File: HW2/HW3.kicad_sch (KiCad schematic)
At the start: 14 parts, among them SW1 SW_Push, SW2 SW_Push, U1 PIC32MX170F256B, U2 AP7381-33, U3 USB-UART

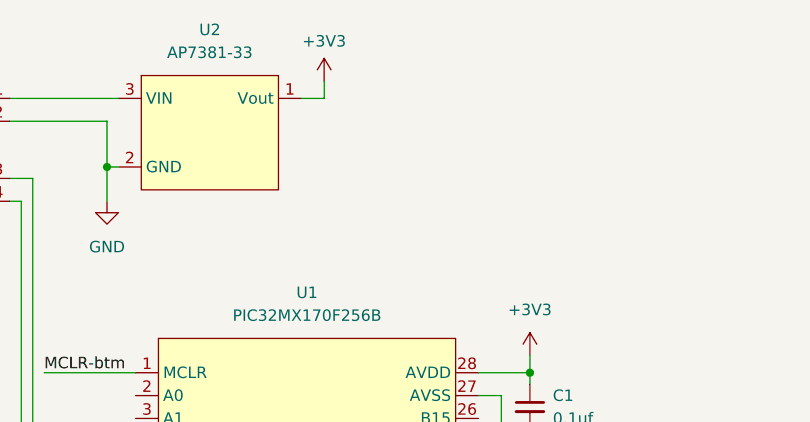
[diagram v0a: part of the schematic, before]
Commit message: HW4 question answered except for last one
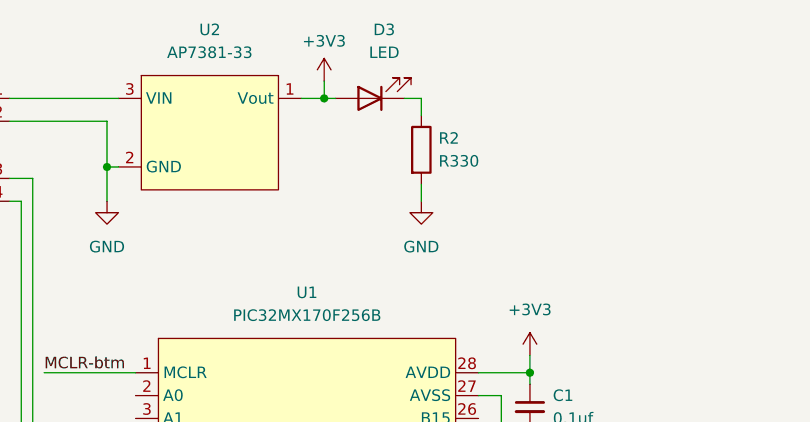
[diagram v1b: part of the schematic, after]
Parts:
- added D3: LED, symbol Device:LED
- added R2: R330, symbol Device:R
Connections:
- net +3V3: now also D3.2 (A)
- net GND: now also R2.2
- new net: D3.1 (K), R2.1
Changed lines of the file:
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@@
   (junction (at 86.36 31.115) (diameter 0) (color 0 0 0 0)
   )
+  (junction (at 110.49 23.495) (diameter 0) (color 0 0 0 0)
+  )
   (junction (at 69.215 84.455) (diameter 0) (color 0 0 0 0)
   )
@@
     (stroke (width 0) (type default))
   )
+  (wire (pts (xy 110.49 23.495) (xy 111.76 23.495))
+    (stroke (width 0) (type default))
+  )
+  (wire (pts (xy 119.38 23.495) (xy 121.285 23.495))
+    (stroke (width 0) (type default))
+  )
   (wire (pts (xy 81.28 81.915) (xy 89.535 81.915))
     (stroke (width 0) (type default))
@@
     (stroke (width 0) (type default))
   )
+  (wire (pts (xy 121.285 33.02) (xy 121.285 34.925))
+    (stroke (width 0) (type default))
+  )
   (wire (pts (xy 133.35 61.595) (xy 133.35 60.325))
     (stroke (width 0) (type default))
@@
   )
   (wire (pts (xy 25.4 93.98) (xy 25.4 95.885))
+    (stroke (width 0) (type default))
+  )
+  (wire (pts (xy 121.285 23.495) (xy 121.285 25.4))
     (stroke (width 0) (type default))
   )
@@
         (path "/4523451e-2353-41a2-8b5b-7b75088095d6"
           (reference "#PWR013") (unit 1)
+        )
+      )
+    )
+  )
+  (symbol (lib_id "Device:R") (at 121.285 29.21 0) (unit 1)
+    (in_bom yes) (on_board yes) (dnp no) (fields_autoplaced)
+    (property "Reference" "R2" (at 123.19 27.94 0)
+      (effects (font (size 1.27 1.27)) (justify left))
+    )
+    (property "Value" "R330" (at 123.19 30.48 0)
+      (effects (font (size 1.27 1.27)) (justify left))
+    )
+    (property "Footprint" "" (at 119.507 29.21 90)
+      (effects (font (size 1.27 1.27)) hide)
+    )
+    (property "Datasheet" "~" (at 121.285 29.21 0)
+      (effects (font (size 1.27 1.27)) hide)
+    )
+    (pin "2")
+    (pin "1")
+    (instances
+      (project "HW3"
+        (path "/4523451e-2353-41a2-8b5b-7b75088095d6"
+          (reference "R2") (unit 1)
         )
       )
@@
     )
   )
+  (symbol (lib_id "Device:LED") (at 115.57 23.495 180) (unit 1)
+    (in_bom yes) (on_board yes) (dnp no) (fields_autoplaced)
+    (property "Reference" "D3" (at 117.1575 15.875 0)
+      (effects (font (size 1.27 1.27)))
+    )
+    (property "Value" "LED" (at 117.1575 18.415 0)
+      (effects (font (size 1.27 1.27)))
+    )
+    (property "Footprint" "" (at 115.57 23.495 0)
+      (effects (font (size 1.27 1.27)) hide)
+    )
+    (property "Datasheet" "~" (at 115.57 23.495 0)
+      (effects (font (size 1.27 1.27)) hide)
+    )
+    (pin "2")
+    (pin "1")
+    (instances
+      (project "HW3"
+        (path "/4523451e-2353-41a2-8b5b-7b75088095d6"
+          (reference "D3") (unit 1)
+        )
+      )
+    )
+  )
   (symbol (lib_id "Device:R") (at 27.305 35.56 0) (unit 1)
     (in_bom yes) (on_board yes) (dnp no) (fields_autoplaced)
@@
         )
       )
+    )
+  )
+  (symbol (lib_id "power:GND") (at 121.285 34.925 0) (unit 1)
+    (in_bom yes) (on_board yes) (dnp no) (fields_autoplaced)
+    (property "Reference" "#PWR015" (at 121.285 41.275 0)
+      (effects (font (size 1.27 1.27)) hide)
+    )
+    (property "Value" "GND" (at 121.285 40.005 0)
+      (effects (font (size 1.27 1.27)))
+    )
+    (property "Footprint" "" (at 121.285 34.925 0)
+      (effects (font (size 1.27 1.27)) hide)
+    )
+    (property "Datasheet" "" (at 121.285 34.925 0)
+      (effects (font (size 1.27 1.27)) hide)
+    )
+    (pin "1")
+    (instances
+      (project "HW3"
+        (path "/4523451e-2353-41a2-8b5b-7b75088095d6"
+          (reference "#PWR015") (unit 1)
+        )
+      )
